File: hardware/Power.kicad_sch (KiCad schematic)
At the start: 20 parts

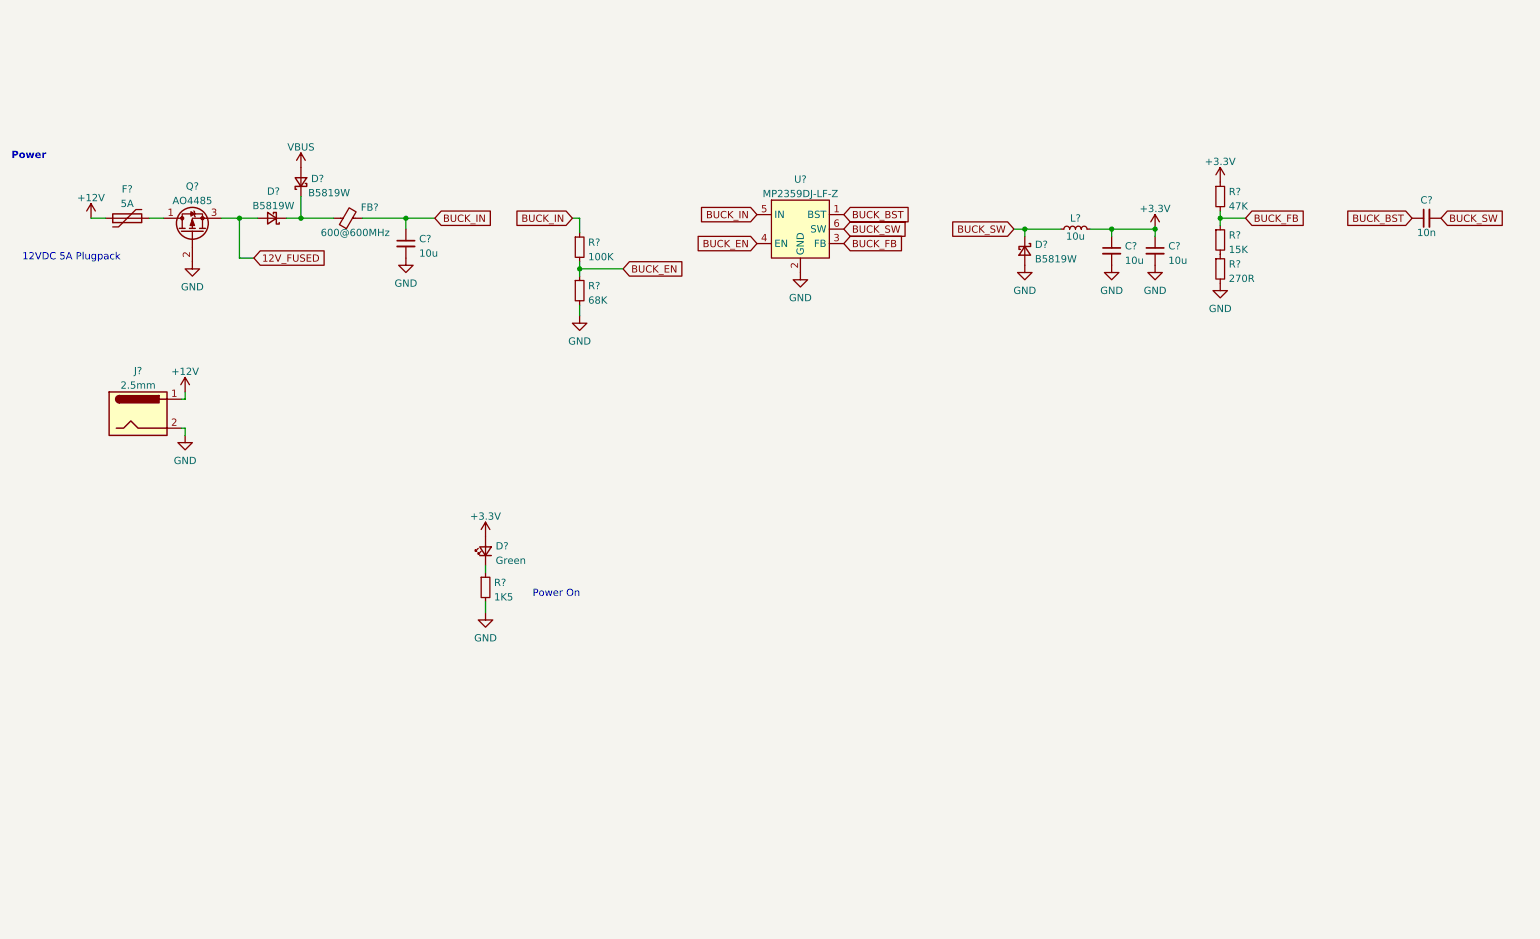
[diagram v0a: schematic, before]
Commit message: schematics finished, footprints assigned. Still need to fix foorptints for MOSFETS
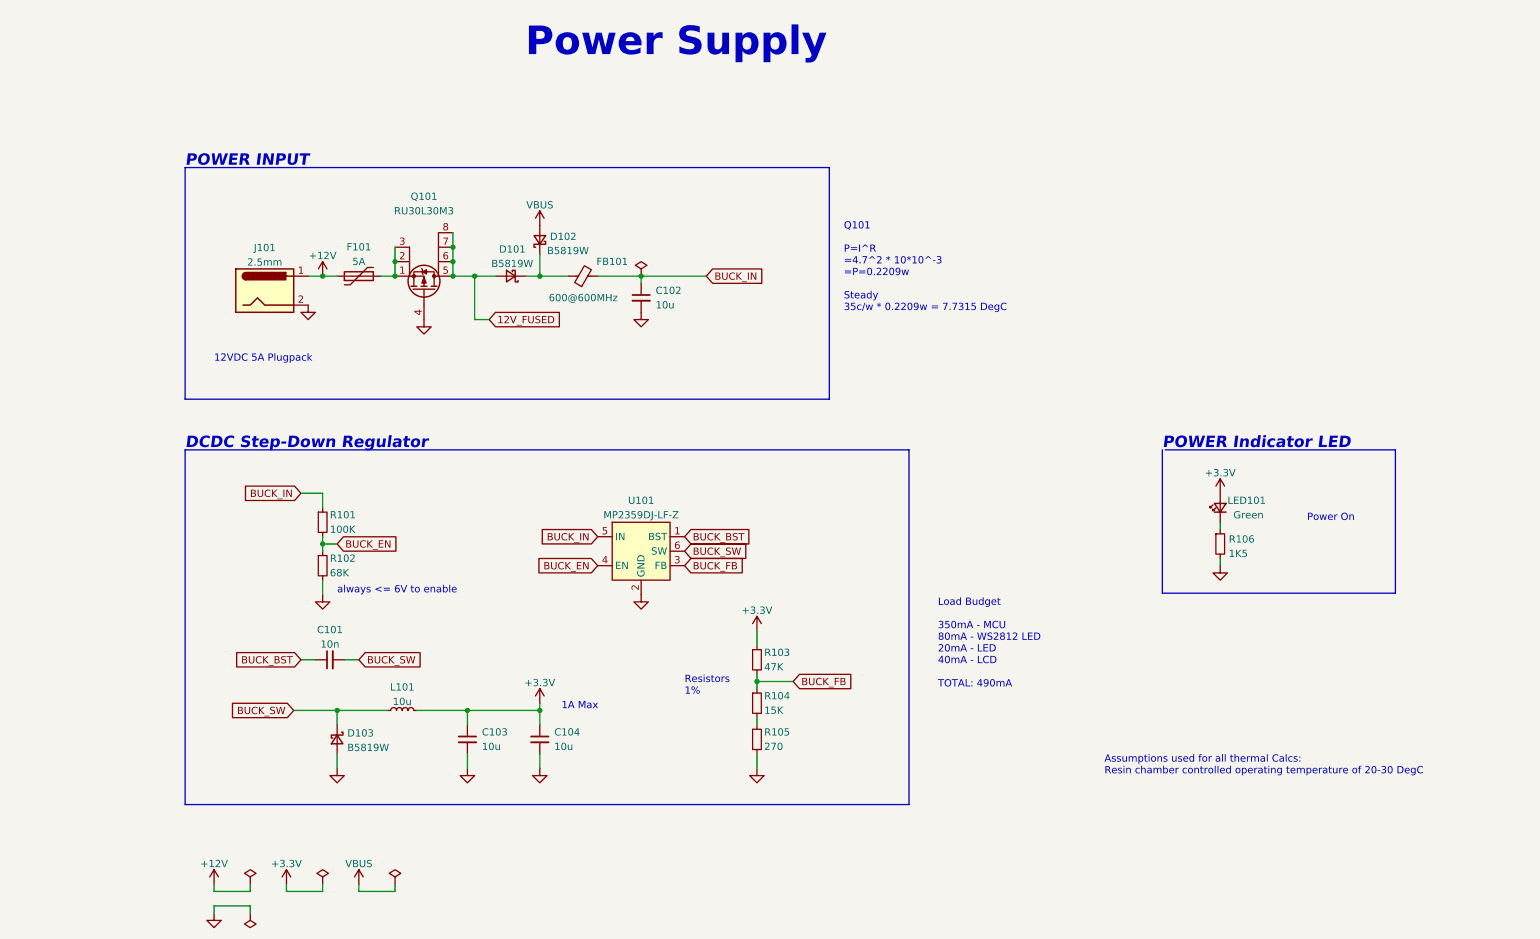
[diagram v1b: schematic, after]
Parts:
- removed C? (x2): 10u, symbol Device:C_Small
- removed C?: 10n, symbol Device:C_Small
- removed D?: Green, symbol Device:LED_Small
- removed D?: B5819W, symbol Device:D_Schottky_Small
- removed L?: 10u, symbol Device:L_Small
- removed Q?: AO4485, symbol Device:Q_PMOS_DGS
- removed R?: 270R, symbol Device:R_Small
- removed R?: 15K, symbol Device:R_Small
- removed R?: 100K, symbol Device:R_Small
- removed R?: 68K, symbol Device:R_Small
- removed R?: 1K5, symbol Device:R_Small
- removed R?: 47K, symbol Device:R_Small
- removed U?: MP2359DJ-LF-Z, Package_TO_SOT_SMD:SOT-23-6, symbol STR-DCDC:MP2359DJ-LF-Z
- added C101: 10n, Capacitor_SMD:C_0603_1608Metric, symbol Device:C_Small
- added C103, C104: 10u, Capacitor_SMD:C_1206_3216Metric, symbol Device:C_Small
- added D103: B5819W, Diode_SMD:D_SOD-123, symbol Device:D_Schottky_Small
- added L101: 10u, Inductor_SMD:L_Sunlord_MWSA0518_5.4x5.2mm, symbol Device:L_Small
- added LED101: Green, LED_SMD:LED_0603_1608Metric, symbol STR-LED:Green
- added Q101: RU30L30M3, Package_DFN_QFN:DFN-8-1EP_3x3mm_P0.65mm_EP1.7x2.05mm, symbol STR-MOSFETS:RU30L30M3
- added R101: 100K, Resistor_SMD:R_0603_1608Metric, symbol Device:R_Small
- added R102: 68K, Resistor_SMD:R_0603_1608Metric, symbol Device:R_Small
- added R103: 47K, Resistor_SMD:R_0603_1608Metric, symbol Device:R_Small
- added R104: 15K, Resistor_SMD:R_0603_1608Metric, symbol Device:R_Small
- added R105: 270, Resistor_SMD:R_0603_1608Metric, symbol Device:R_Small
- added R106: 1K5, Resistor_SMD:R_0603_1608Metric, symbol Device:R_Small
- added U101: MP2359DJ-LF-Z, Package_TO_SOT_SMD:SOT-23-6, symbol STR-DCDC:MP2359DJ-LF-Z
- C102: renamed from C?; footprint (none) -> Capacitor_SMD:C_1206_3216Metric
- D101, D102: renamed from D?; footprint (none) -> Diode_SMD:D_SOD-123; LCSC (none) -> C8598
- F101: renamed from F?; symbol STR-Fuses:F1206HI8000V024TM -> STR-Fuses:F1206HI5000V032TM; LCSC (none) -> C226251; MANUFACTURER (none) -> AEM; MFPN F1206HI8000V024TM -> F1206HI5000V032TM
- FB101: renamed from FB?; footprint (none) -> Inductor_SMD:L_0805_2012Metric; LCSC (none) -> C1017
- J101: renamed from J?; footprint (none) -> Connector_BarrelJack:BarrelJack_CUI_PJ-036AH-SMT_Horizontal
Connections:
- net +3V3: now also C103.1, C104.1, L101.2, LED101.2 (A), R103.1
- net 12V_FUSED: now also Q101.5 (D), Q101.6 (D), Q101.7 (D), Q101.8 (D)
- net BUCK_BST: now also C101.1, U101.1 (BST)
- net BUCK_EN: now also R101.2, R102.1, U101.4 (EN)
- net BUCK_FB: now also R103.2, R104.1, U101.3 (FB)
- net BUCK_IN: now also R101.1, U101.5 (IN)
- net BUCK_SW: now also C101.2, D103.1 (K), L101.1, U101.6 (SW)
- net GND: now also C103.2, C104.2, D103.2 (A), Q101.4 (G), R102.2, R105.2, R106.2, U101.2 (GND)
- net at F101.2: now also Q101.1 (S), Q101.2 (S), Q101.3 (S)
- new net: R104.2, R105.1
- new net: LED101.1 (K), R106.1
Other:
- note added: "1A Max"
- note added: "Assumptions used for all thermal Calcs: Resin chamber controlled operating temperature of 20-30 DegC"
- note added: "DCDC Step-Down Regulator"
- note added: "Load Budget 350mA - MCU 80mA - WS2812 LED 20mA - LED 40mA - LCD TOTAL: 490mA"
- note added: "POWER INPUT"
- note added: "POWER Indicator LED"
- note added: "Power Supply"
- note added: "Q101 P=I^R =4.7^2 * 10*10^-3 =P=0.2209w Steady 35c/w * 0.2209w = 7.7315 DegC"
- note added: "Resistors 1%"
- note added: "always <= 6V to enable"
- note removed: "Power"
- title: (none) -> SLA Chamber Hearter for Resin Printers
- moved on the sheet: C102, D101, D102, F101, FB101, J101

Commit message: footprint update for MOSFETS to PDFN3333
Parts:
- Q101: footprint Package_DFN_QFN:DFN-8-1EP_3x3mm_P0.65mm_EP1.7x2.05mm -> STR-DFN:PDFN3333
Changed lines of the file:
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@@
     (property "Reference" "Q101" (id 0) (at 90.17 58.42 90))
     (property "Value" "RU30L30M3" (id 1) (at 90.17 60.96 90))
-    (property "Footprint" "Package_DFN_QFN:DFN-8-1EP_3x3mm_P0.65mm_EP1.7x2.05mm" (id 2) (at 88.265 69.85 0)
+    (property "Footprint" "STR-DFN:PDFN3333" (id 2) (at 88.265 69.85 0)
       (effects (font (size 1.27 1.27) italic) (justify left) hide)
     )

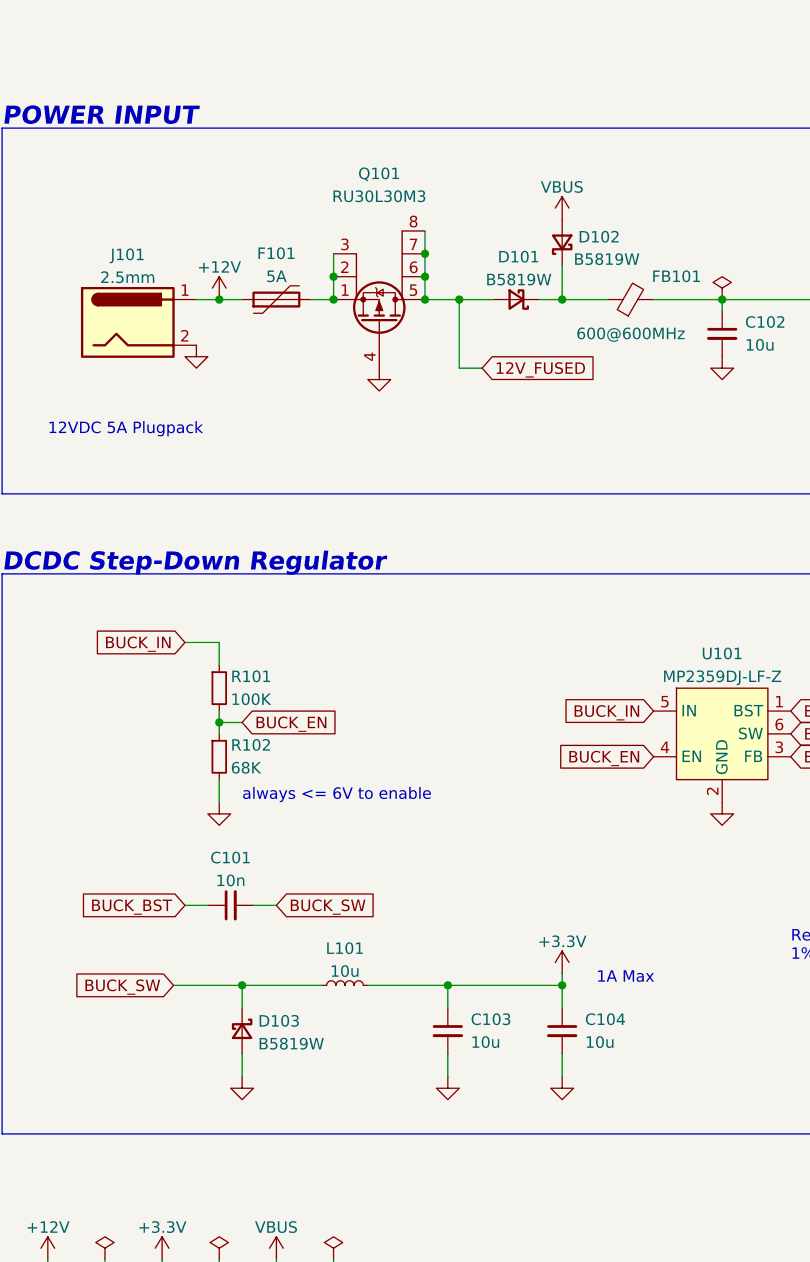
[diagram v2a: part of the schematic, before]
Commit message: routing and foot print changes
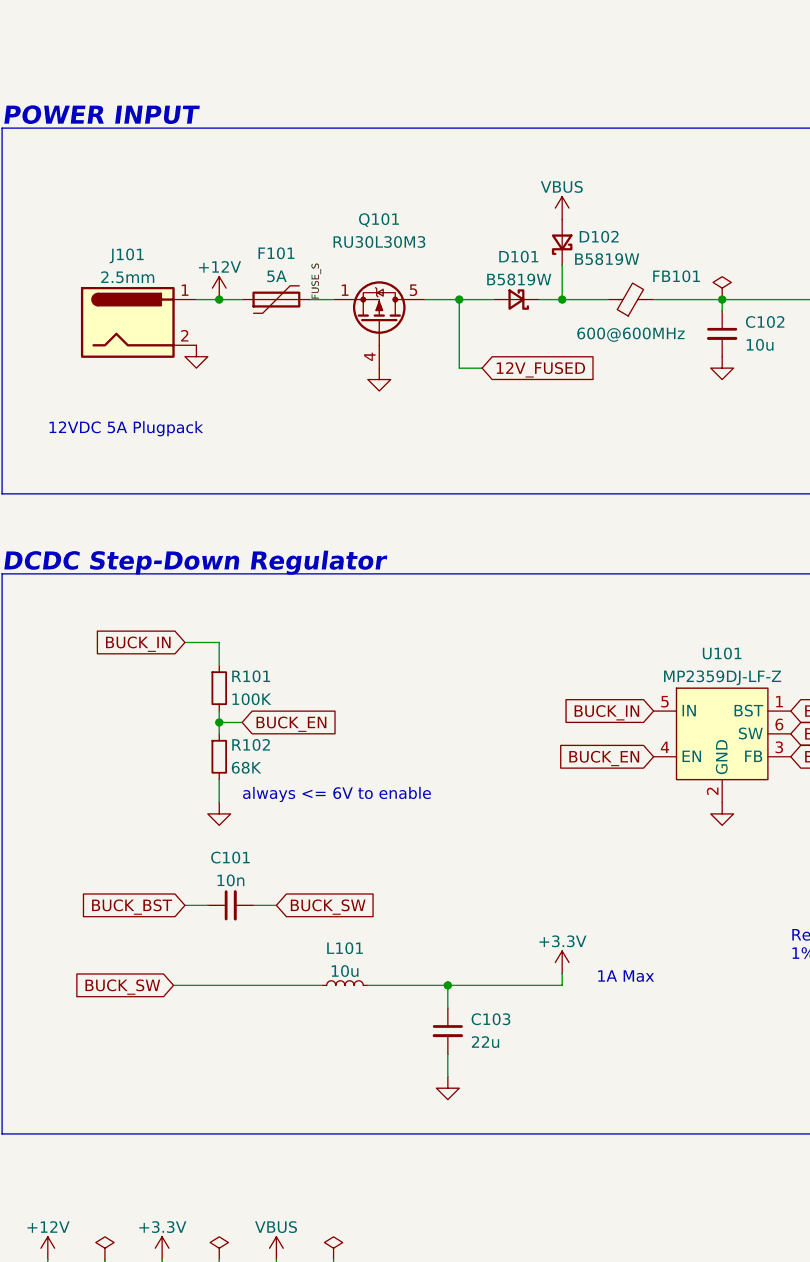
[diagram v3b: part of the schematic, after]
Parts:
- removed C104: 10u, Capacitor_SMD:C_1206_3216Metric, symbol Device:C_Small
- removed D103: B5819W, Diode_SMD:D_SOD-123, symbol Device:D_Schottky_Small
- C101: footprint Capacitor_SMD:C_0603_1608Metric -> Capacitor_SMD:C_0402_1005Metric
- C102: footprint Capacitor_SMD:C_1206_3216Metric -> Capacitor_SMD:C_0603_1608Metric
- C103: value 10u -> 22u; footprint Capacitor_SMD:C_1206_3216Metric -> Capacitor_SMD:C_0603_1608Metric
- J101: footprint Connector_BarrelJack:BarrelJack_CUI_PJ-036AH-SMT_Horizontal -> TerminalBlock_Phoenix:TerminalBlock_Phoenix_PT-1,5-2-3.5-H_1x02_P3.50mm_Horizontal
- Q101: footprint STR-DFN:PDFN3333 -> STR-DFN:DFN-8_L3.0-W3.0-P0.65-BL; symbol STR-MOSFETS:RU30L30M3 -> STR-MOSFETS:RU3030M3
- R101, R102, R103, R104, R105, R106: footprint Resistor_SMD:R_0603_1608Metric -> Resistor_SMD:R_0402_1005Metric
- U101: footprint Package_TO_SOT_SMD:SOT-23-6 -> STR-DFN:SOT-23-6_L2.9-W1.6-P0.95-LS2.8-BL
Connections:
- net 12V_FUSED: now also Q101.9 (D)
- net FUSE_S: now reaches F101.2, Q101.1 (S), Q101.2 (S), Q101.3 (S)
